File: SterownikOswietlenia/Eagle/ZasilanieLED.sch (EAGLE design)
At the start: 24 parts, among them Q1 SPD30P06PTO252, Q2 SPD30P06PTO252, Q3 SPD30P06PTO252, T1 BC847, T2 BC847, T3 BC847, U1 WS2801, X1 5569-02, X2 5569-02, X3 5569-02, X4 5569-08, X5 5569-08

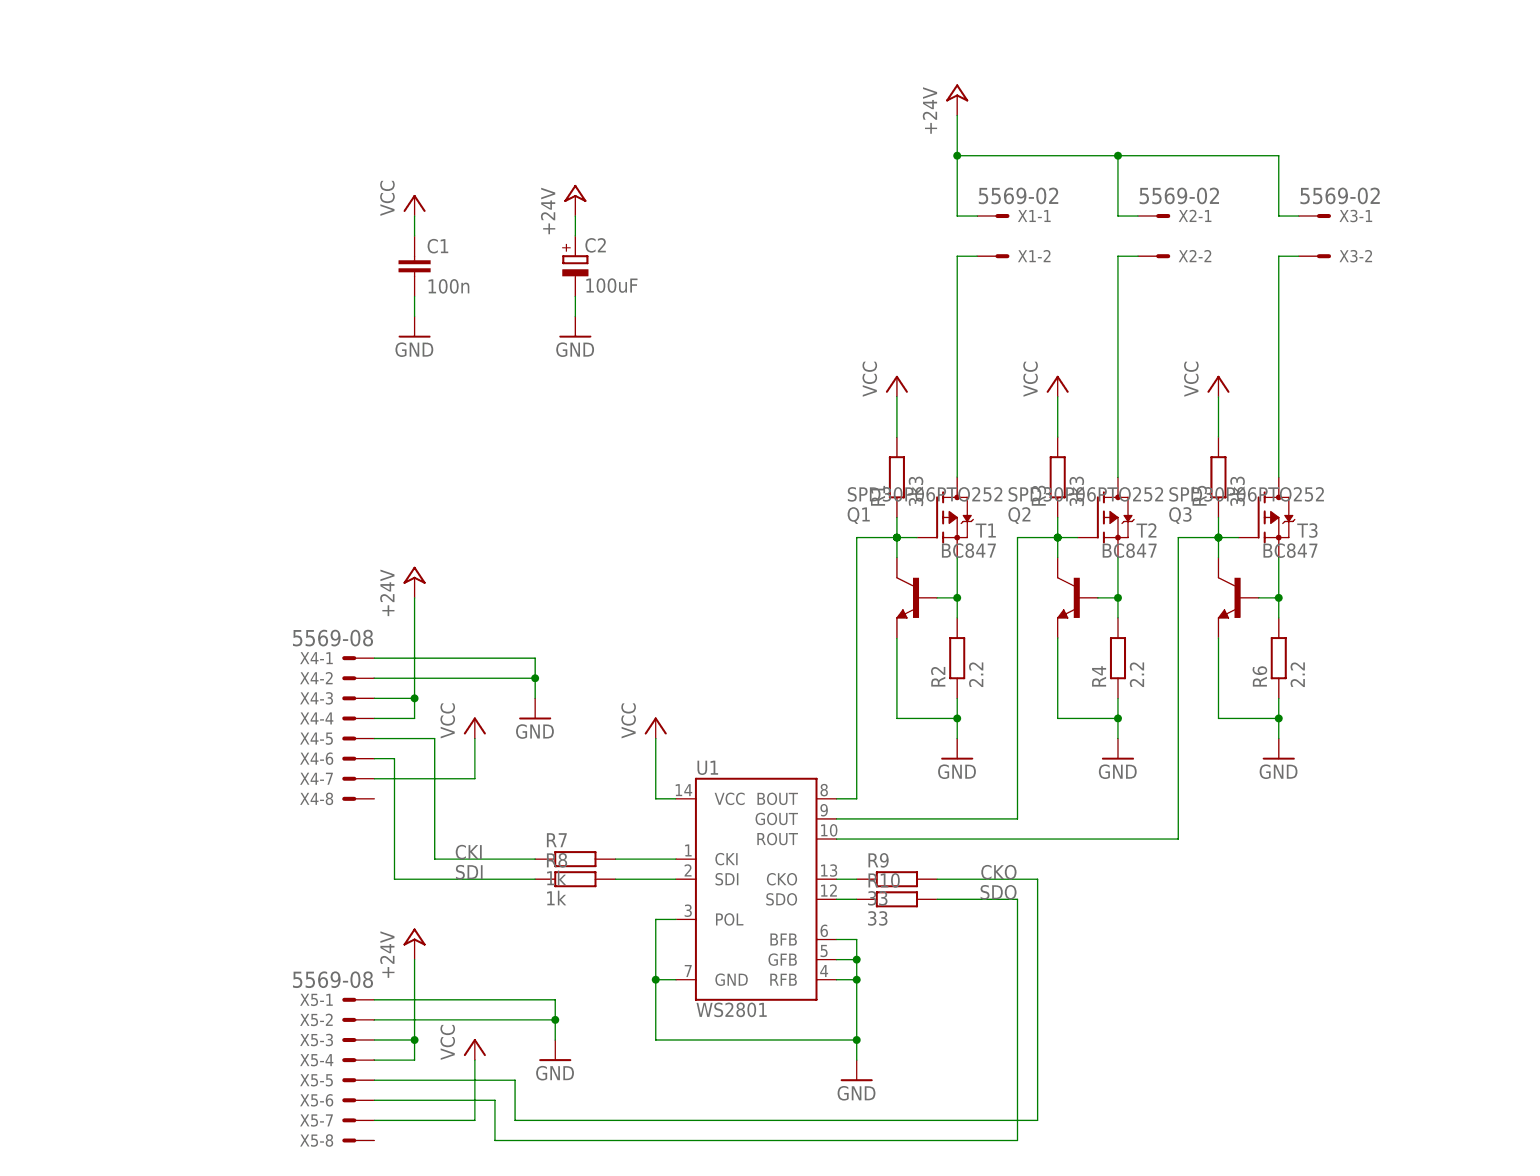
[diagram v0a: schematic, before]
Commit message: uporzą▲dkowane opisy elementów
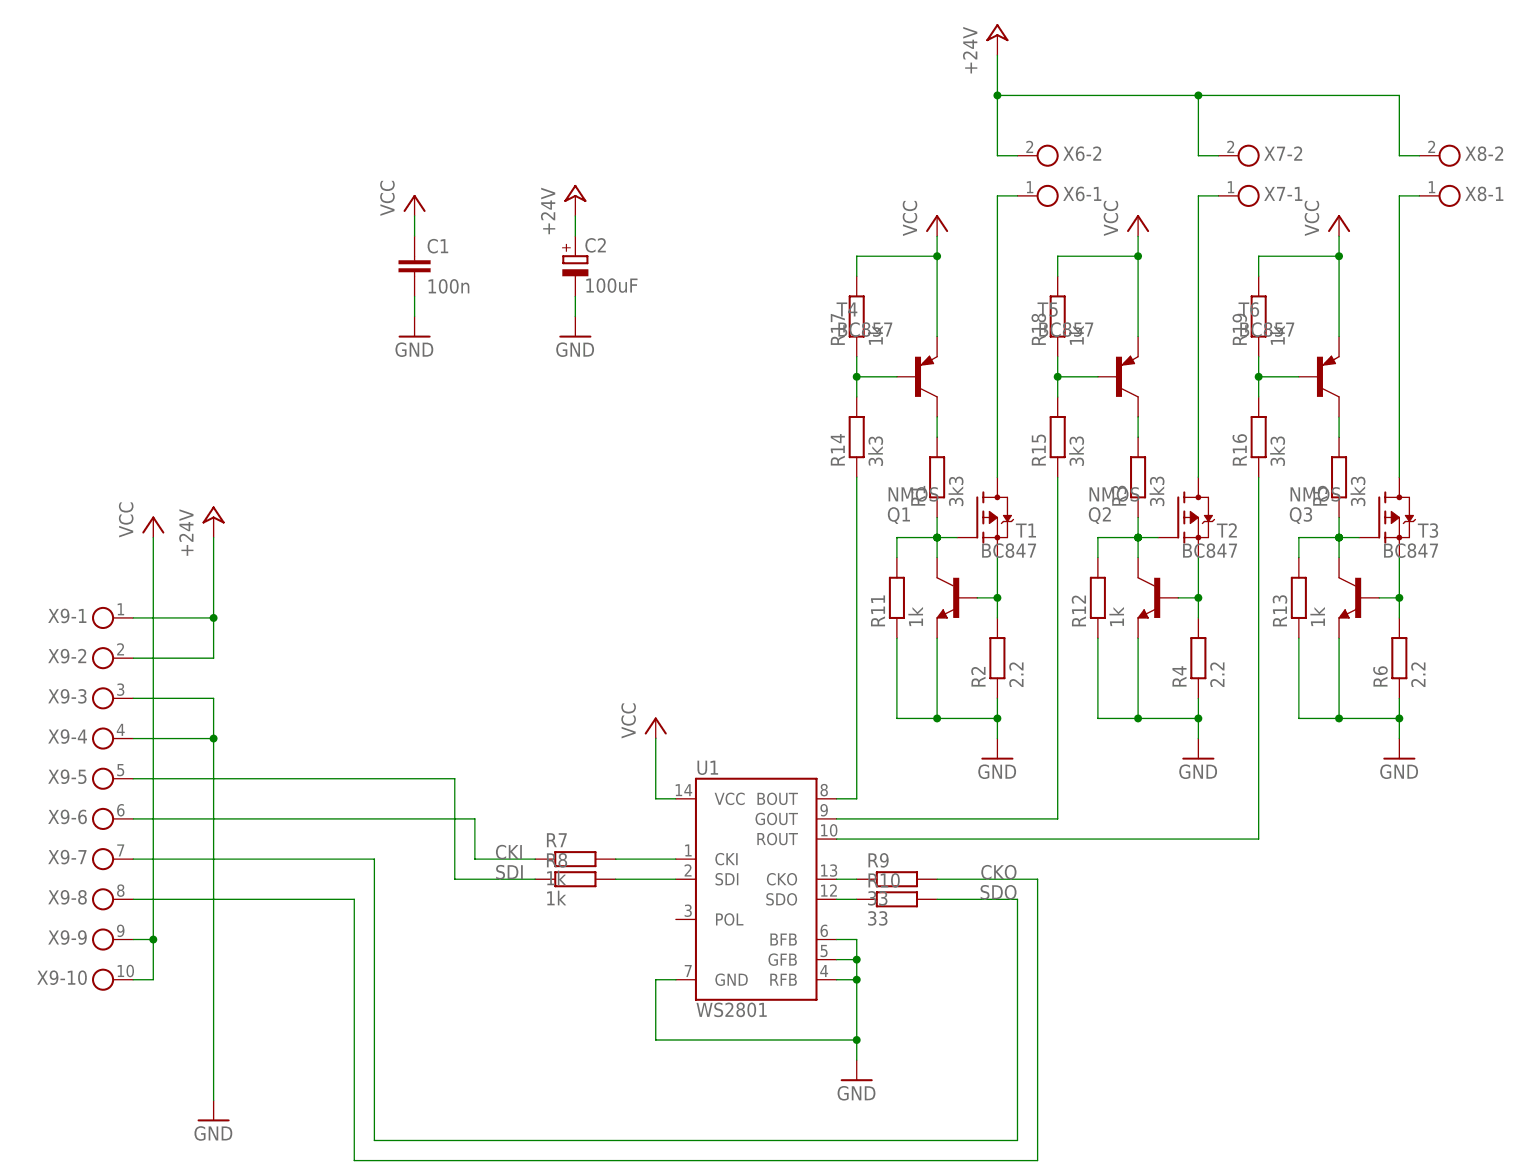
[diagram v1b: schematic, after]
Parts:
- removed X1, X2, X3: 5569-02, con-molex-5569:5569-02
- removed X4, X5: 5569-08, con-molex-5569:5569-08
- added R11, R12, R13, R17, R18, R19: 1k, rcl:R-EU_R1206
- added R14, R15, R16: 3k3, rcl:R-EU_R1206
- added T4, T5, T6: BC857, transistor:BC857A-PNP-SOT23-BEC
- added X6, X7, X8: (no value), con-ria-59:AKL59-02
- added X9: (no value), con-ria-59:AKL59-10
- C2: device rcl:CPOL-EUE35-12AXIAL -> rcl:CPOL-EUE5-10.5
- Q1, Q2, Q3: value SPD30P06PTO252 -> NMOS
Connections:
- new net N$14: R1.2, T4.C
- new net N$15: R3.2, T5.C
- new net N$16: R5.2, T6.C
- new net N$17: Q1.G, R1.1, R11.2, T1.C
- new net N$18: Q2.G, R12.2, R3.1, T2.C
- new net N$19: Q3.G, R13.2, R5.1, T3.C
- new net N$20: R14.2, R17.1, T4.B
- new net N$21: R15.2, R18.1, T5.B
- new net N$22: R16.2, R19.1, T6.B
- net +24V: now also X6-2.1, X7-2.1, X8-2.1, X9-1.1, X9-2.1; no longer X1-1.>NAME$, X2-1.>NAME$, X3-1.>NAME$, X4-3.>NAME$, X4-4.>NAME$, X5-3.>NAME$, X5-4.>NAME$
- net CKI: now also X9-6.1; no longer X4-5.>NAME$
- net CKO: now also X9-8.1; no longer X5-5.>NAME$
- net GND: now also R11.1, R12.1, R13.1, X9-3.1, X9-4.1; no longer U1.POL, X4-1.>NAME$, X4-2.>NAME$, X5-1.>NAME$, X5-2.>NAME$
- net N$11: now also X6-1.1; no longer X1-2.>NAME$
- net N$12: now also X7-1.1; no longer X2-2.>NAME$
- net N$13: now also X8-1.1; no longer X3-2.>NAME$
- net N$4: now also R14.1; no longer Q1.G, R1.1, T1.C
- net N$5: now also R15.1; no longer Q2.G, R3.1, T2.C
- net N$6: now also R16.1; no longer Q3.G, R5.1, T3.C
- net SDI: now also X9-5.1; no longer X4-6.>NAME$
- net SDO: now also X9-7.1; no longer X5-6.>NAME$
- net VCC: now also R17.2, R18.2, R19.2, T4.E, T5.E, T6.E, X9-10.1, X9-9.1; no longer R1.2, R3.2, R5.2, X4-7.>NAME$, X5-7.>NAME$
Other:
- moved on the sheet: Q1, Q2, Q3, R1, R2, R3, R4, R5, R6, T1, T2, T3
